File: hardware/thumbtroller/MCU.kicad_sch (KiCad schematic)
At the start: 28 parts, among them J2 UART, J9 Conn_02x03, U5 ESP32-H2-MINI-1

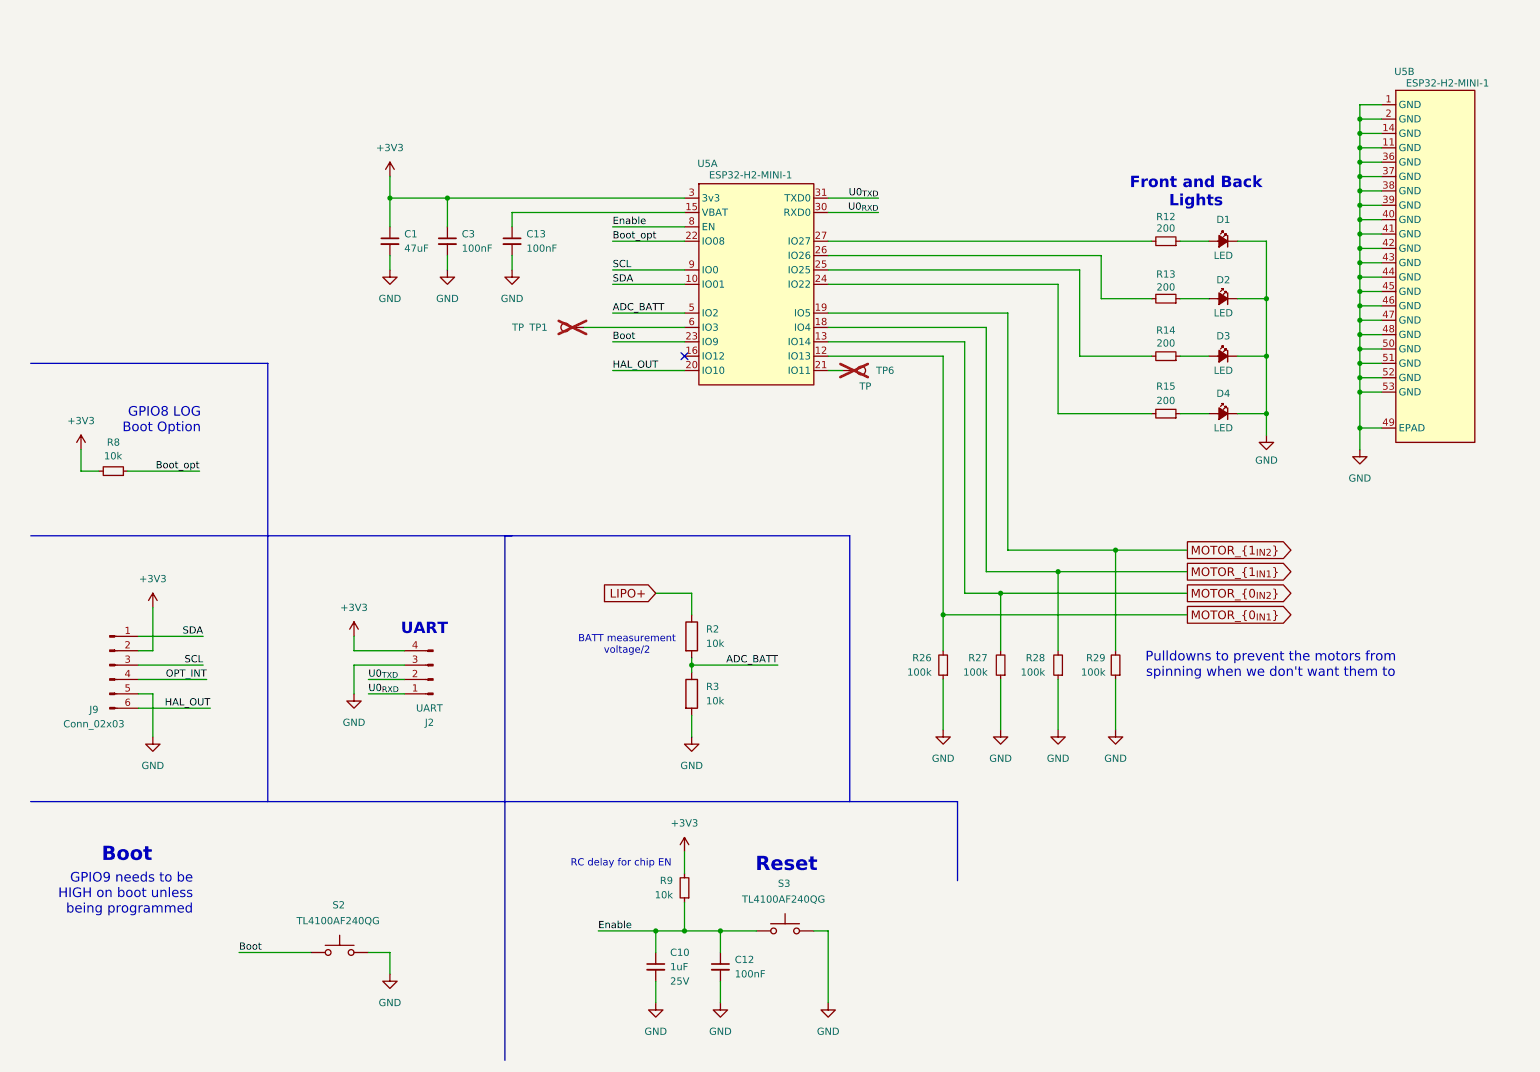
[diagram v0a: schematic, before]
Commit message: Schematic readability update
Updated Schematics to hierarchical, Schematic size to A4.
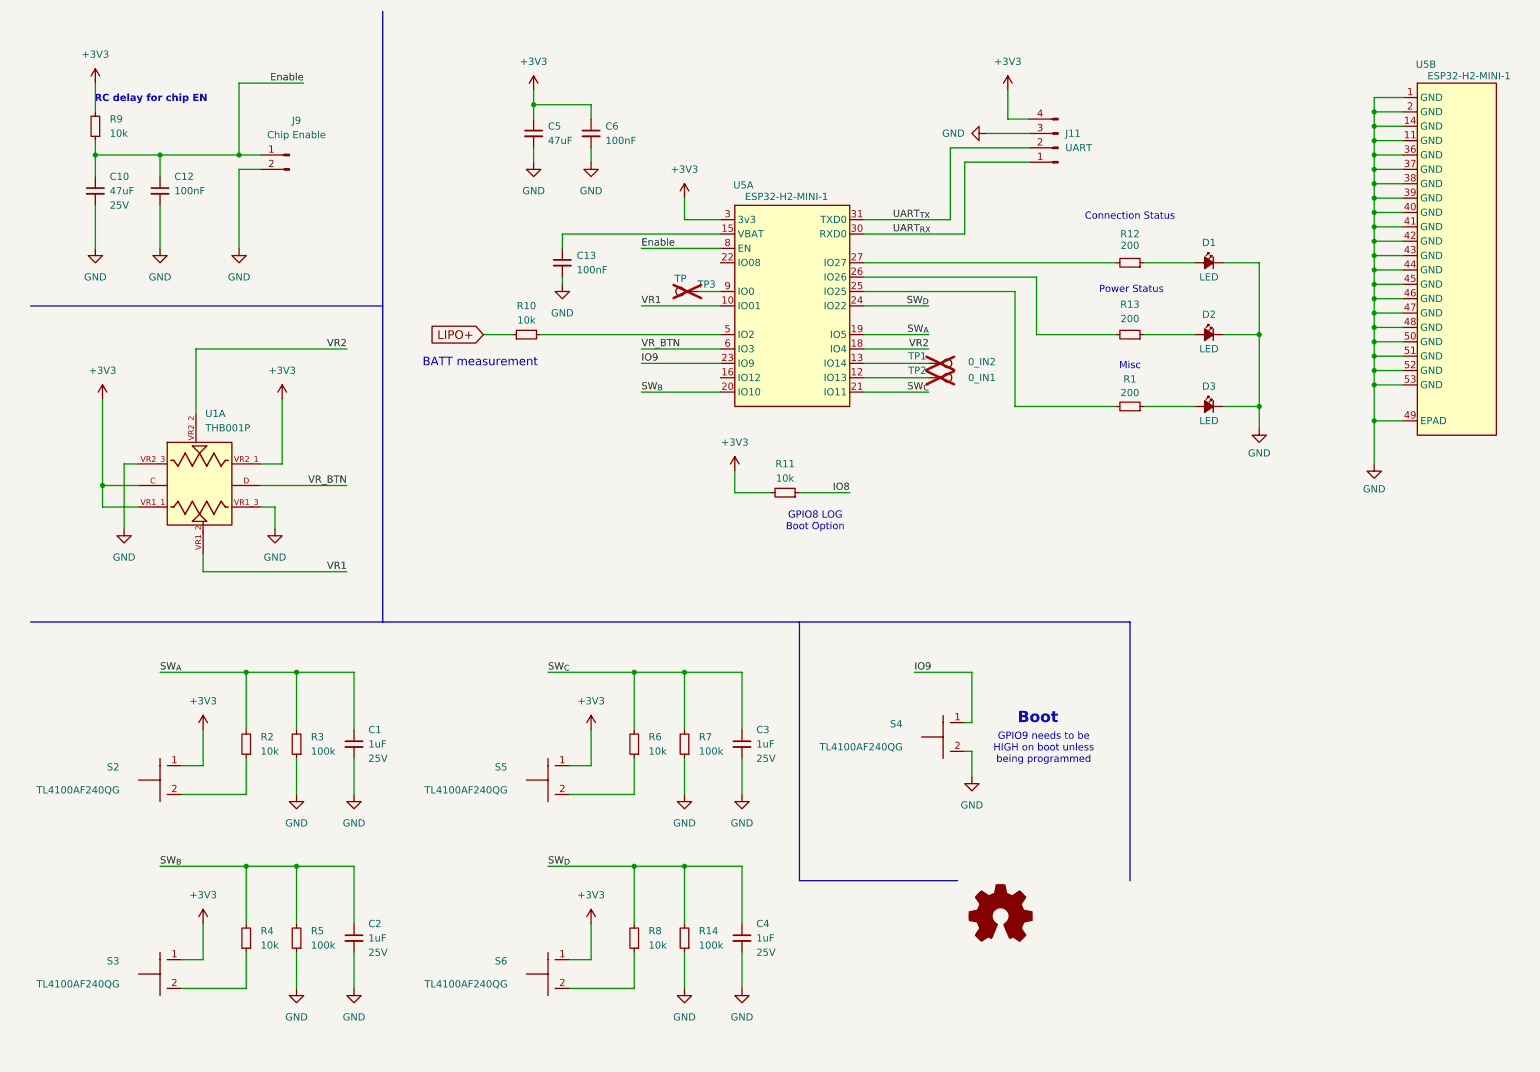
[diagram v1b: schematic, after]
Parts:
- removed D4: LED, Capacitor_SMD:C_0603_1608Metric, symbol Device:LED_Small_Filled
- removed J2: UART, Connector_PinHeader_2.54mm:PinHeader_1x04_P2.54mm_Vertical, symbol Connector:Conn_01x04_Male
- removed J9: Conn_02x03, Connector_PinHeader_1.27mm:PinHeader_2x03_P1.27mm_Vertical_SMD, symbol Connector:Conn_01x06_Pin
- removed R15: 200, Resistor_SMD:R_0603_1608Metric, symbol Device:R_Small
- removed R2, R3: 10k, Resistor_SMD:R_0603_1608Metric, symbol Device:R
- removed R26, R27, R28, R29: 100k, Resistor_SMD:R_0603_1608Metric, symbol Device:R_Small
- removed S2, S3: TL4100AF240QG, Button_Switch_THT:SW_PUSH_6mm, symbol Switch:SW_Omron_B3FS
- removed TP6: TP, TestPoint:TestPoint_Pad_D1.0mm, symbol Connector:TestPoint
- added C2, C4: 1uF, Capacitor_SMD:C_0603_1608Metric, symbol Device:C_Small
- added C5: 47uF, Capacitor_SMD:C_0603_1608Metric, symbol Device:C_Small
- added C6: 100nF, Capacitor_SMD:C_0603_1608Metric, symbol Device:C_Small
- added J11: UART, Connector_PinHeader_2.54mm:PinHeader_1x04_P2.54mm_Vertical, symbol Connector:Conn_01x04_Male
- added J9: Chip Enable, Connector_PinHeader_2.54mm:PinHeader_1x02_P2.54mm_Vertical, symbol Connector:Conn_01x02_Male
- added R1: 200, Resistor_SMD:R_0603_1608Metric, symbol Device:R_Small
- added R10, R11, R2, R4, R6: 10k, Resistor_SMD:R_0603_1608Metric, symbol Device:R_Small
- added R3, R5, R7: 100k, Resistor_SMD:R_0603_1608Metric, symbol Device:R_Small
- added S2, S3, S4, S5, S6: TL4100AF240QG, kicad_reformed_custom_IC:SW_PTS810_SJM_250_SMTR_LFS, symbol custom_IC:TL4100AF240QG_
- added TP2: 0_IN1, TestPoint:TestPoint_Pad_1.0x1.0mm, symbol Connector:TestPoint
- added TP3: TP, TestPoint:TestPoint_Pad_D1.0mm, symbol Connector:TestPoint
- added U1: THB001P, kicad_reformed_custom_IC:CNK_THB001P, symbol custom_IC:THB001P
- C1: value 47uF -> 1uF; footprint (none) -> Capacitor_SMD:C_0603_1608Metric
- C10: value 1uF -> 47uF; footprint (none) -> Capacitor_SMD:C_0603_1608Metric
- C12: footprint (none) -> Capacitor_SMD:C_0603_1608Metric
- C13: footprint (none) -> Capacitor_SMD:C_0603_1608Metric; Voltage 25V -> (none)
- C3: value 100nF -> 1uF; footprint (none) -> Capacitor_SMD:C_0603_1608Metric
- R14: value 200 -> 100k
- TP1: value TP -> 0_IN2; footprint TestPoint:TestPoint_Pad_D1.0mm -> TestPoint:TestPoint_Pad_1.0x1.0mm
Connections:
- net MOTOR_{0_{IN2}} is gone; now on an unnamed net: U5.13 (IO14)
- net +3V3: now also C5.1, C6.1, J11.4 (Pin_4), R11.2, S2.1, S3.1, S5.1, S6.1, U1.C, U1.VR1_1, U1.VR2_1; no longer C1.1, C3.1, R8.2
- net Enable: now also J9.1 (Pin_1)
- net GND: now also R14.1, C2.2, C4.2, C5.2, C6.2, J11.3 (Pin_3), J9.2 (Pin_2), R3.1, R5.1, R7.1, S4.2, U1.VR1_3, U1.VR2_3
- net LIPO+: now also R10.1
- net SW_{C}: now reaches U5.21 (IO11)
- net SW_{C}: now also C3.1, R6.2, R7.2
- net SW_{D}: now reaches U5.24 (IO22)
- net SW_{D}: now also R14.2, R8.2, C4.1
- net at U5.25 (IO25): now also R1.2; no longer R14.2
- net at TP1.1: no longer U5.6 (IO3)
- net at D3.2 (A): now also R1.1; no longer R14.1
- net ADC_BATT: no longer names the net of U5.5 (IO2)
- net ADC_BATT: now also R10.2
- net Boot renamed IO9
- net IO9: now also S4.1
- net Boot_opt: no longer names the net of R8.1
- net Boot_opt: now also S6.2; no longer U5.22 (IO08)
- net HAL_OUT renamed SW_{B}
- net SW_{B}: now also C2.1, R4.2, R5.2
- net MOTOR_{0_{IN1}}: no longer names the net of U5.12 (IO13)
- net MOTOR_{0_{IN1}}: now also TP2.1
- net MOTOR_{1_{IN1}} renamed VR2
- net VR2: now also U1.VR2_2
- net MOTOR_{1_{IN2}} renamed SW_{A}
- net SW_{A}: now also C1.1, R2.2, R3.2
- net SCL: no longer names the net of U5.9 (IO0)
- net SCL: now also TP3.1
- net SDA renamed VR1
- net VR1: now also U1.VR1_2
- net U0_{RXD} renamed UART_{RX}
- net UART_{RX}: now also J11.1 (Pin_1)
- net U0_{TXD} renamed UART_{TX}
- net UART_{TX}: now also J11.2 (Pin_2)
- new net: R2.1, S2.2
- new net: R4.1, S3.2
- new net: R6.1, S5.2
- new net IO8: R11.1
- new net VR_BTN: U1.D, U5.6 (IO3)
- no-connect marks 1 -> 0
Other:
- note added: "BATT measurement"
- note added: "Connection Status"
- note added: "Misc"
- note added: "Power Status"
- note removed: "BATT measurement voltage/2"
- note removed: "Front and Back Lights"
- note removed: "Pulldowns to prevent the motors from spinning when we don't want them to"
- note removed: "Reset"
- note removed: "UART"
- company: (none) -> StuckAtPrototype
- title: (none) -> Thumbtroller
